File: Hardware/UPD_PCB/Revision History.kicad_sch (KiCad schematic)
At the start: 0 parts

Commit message: Finalized version V1.0
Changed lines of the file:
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@@
 		)
 	)
-	(text_box "[${#}] ${TITLE}"
+	(text_box "[${#}] Revision History\n"
 		(exclude_from_sim no)
 		(at 80.01 16.51 0)
@@
 		)
 	)
-	(text_box "- _________________________________\n\n- _________________________________\n\n- _________________________________\n\n- _________________________________\n\n- _________________________________\n\n- _________________________________\n\n- _________________________________\n\n- _________________________________\n\n- _________________________________\n\n- _________________________________\n\n- _________________________________\n\n- _________________________________\n\n- _________________________________\n\n- _________________________________\n\n- _________________________________\n\n- _________________________________\n\n- _________________________________"
+	(text_box "- First prototype is fully made and ordered\n\n\n- Future improvements:\n- Reduce size of components and pcb\n- Improve Input filtering\n- _________________________________\n\n- _________________________________\n\n- _________________________________\n\n- _________________________________\n\n- _________________________________\n\n- _________________________________\n\n- _________________________________\n\n- _________________________________\n\n- _________________________________\n\n- _________________________________\n\n- _________________________________\n\n- _________________________________\n\n- _________________________________"
 		(exclude_from_sim no)
 		(at 22.86 40.64 0)
@@
 		)
 	)
-	(text_box "DD.MM.YYYY - xxx Revision\nVariant: xxx"
+	(text_box "20.03.2025 - V1.0 Revision\nVariant: 1.0"
 		(exclude_from_sim no)
 		(at 20.32 31.75 0)

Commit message: Version 1.1 of PCB
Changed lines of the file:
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@@
 		)
 	)
-	(text_box "DD.MM.YYYY - xxx Revision\nVariant: xxx"
+	(text_box "28.04.2025 - V1.1 Revision\nVariant: 1.1"
 		(exclude_from_sim no)
 		(at 86.36 31.75 0)
@@
 		)
 	)
-	(text_box "- _________________________________\n\n- _________________________________\n\n- _________________________________\n\n- _________________________________\n\n- _________________________________\n\n- _________________________________\n\n- _________________________________\n\n- _________________________________\n\n- _________________________________\n\n- _________________________________\n\n- _________________________________\n\n- _________________________________\n\n- _________________________________\n\n- _________________________________\n\n- _________________________________\n\n- _________________________________\n\n- _________________________________"
+	(text_box "- Changed INA219 16V I²C adress\n\n- Changed footprint for Viout and 5 volt output\n\n- Changed certain traces to be better\n\n- Changed Shunt resistor values to 0.1 Ohm\n\n- _________________________________\n\n- _________________________________\n\n- _________________________________\n\n- _________________________________\n\n- _________________________________\n\n- _________________________________\n\n- _________________________________\n\n- _________________________________\n\n- _________________________________\n\n- _________________________________\n\n- _________________________________\n\n- _________________________________\n\n- _________________________________"
 		(exclude_from_sim no)
 		(at 88.9 40.64 0)

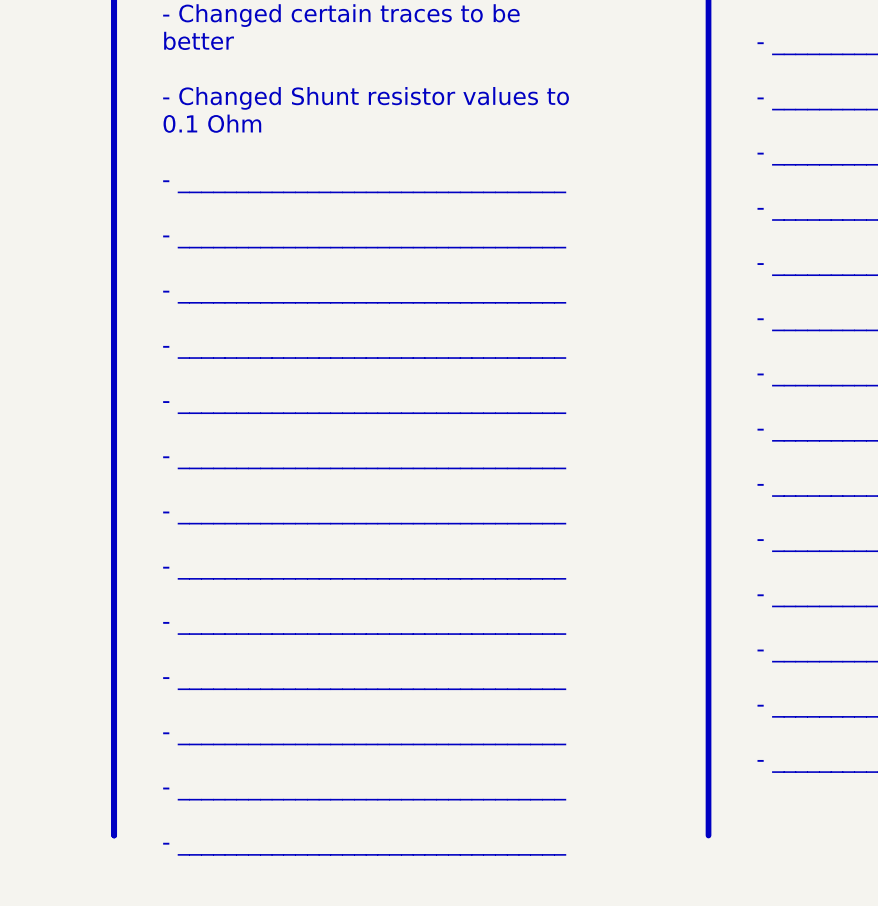
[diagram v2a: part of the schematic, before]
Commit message: Full system monitoring of PCB
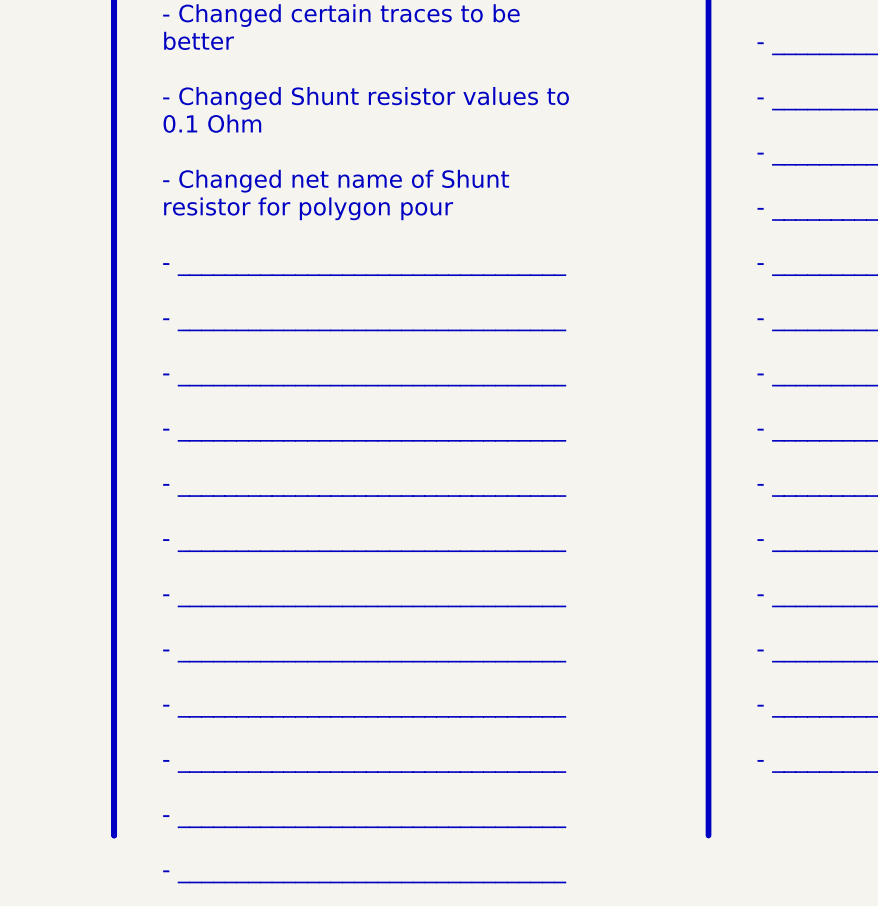
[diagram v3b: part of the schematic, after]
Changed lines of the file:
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@@
 		)
 	)
-	(text_box "- Changed INA219 16V I²C adress\n\n- Changed footprint for Viout and 5 volt output\n\n- Changed certain traces to be better\n\n- Changed Shunt resistor values to 0.1 Ohm\n\n- _________________________________\n\n- _________________________________\n\n- _________________________________\n\n- _________________________________\n\n- _________________________________\n\n- _________________________________\n\n- _________________________________\n\n- _________________________________\n\n- _________________________________\n\n- _________________________________\n\n- _________________________________\n\n- _________________________________\n\n- _________________________________"
+	(text_box "- Changed INA219 16V I²C adress\n\n- Changed footprint for Viout and 5 volt output\n\n- Changed certain traces to be better\n\n- Changed Shunt resistor values to 0.1 Ohm\n\n- Changed net name of Shunt resistor for polygon pour\n\n- _________________________________\n\n- _________________________________\n\n- _________________________________\n\n- _________________________________\n\n- _________________________________\n\n- _________________________________\n\n- _________________________________\n\n- _________________________________\n\n- _________________________________\n\n- _________________________________\n\n- _________________________________\n\n- _________________________________"
 		(exclude_from_sim no)
 		(at 88.9 40.64 0)
